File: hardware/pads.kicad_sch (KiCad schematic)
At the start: 21 parts, among them J10 M3, J13 M4, J20 LED, J21 5V, J22 BZ-, J23 CAM, J24 5V, J25 GND, J26 VHD, J27 GND, J28 TX0, J29 RX0, J31 USB, J32 CAM, J33 GND, J4 M1, J7 M2

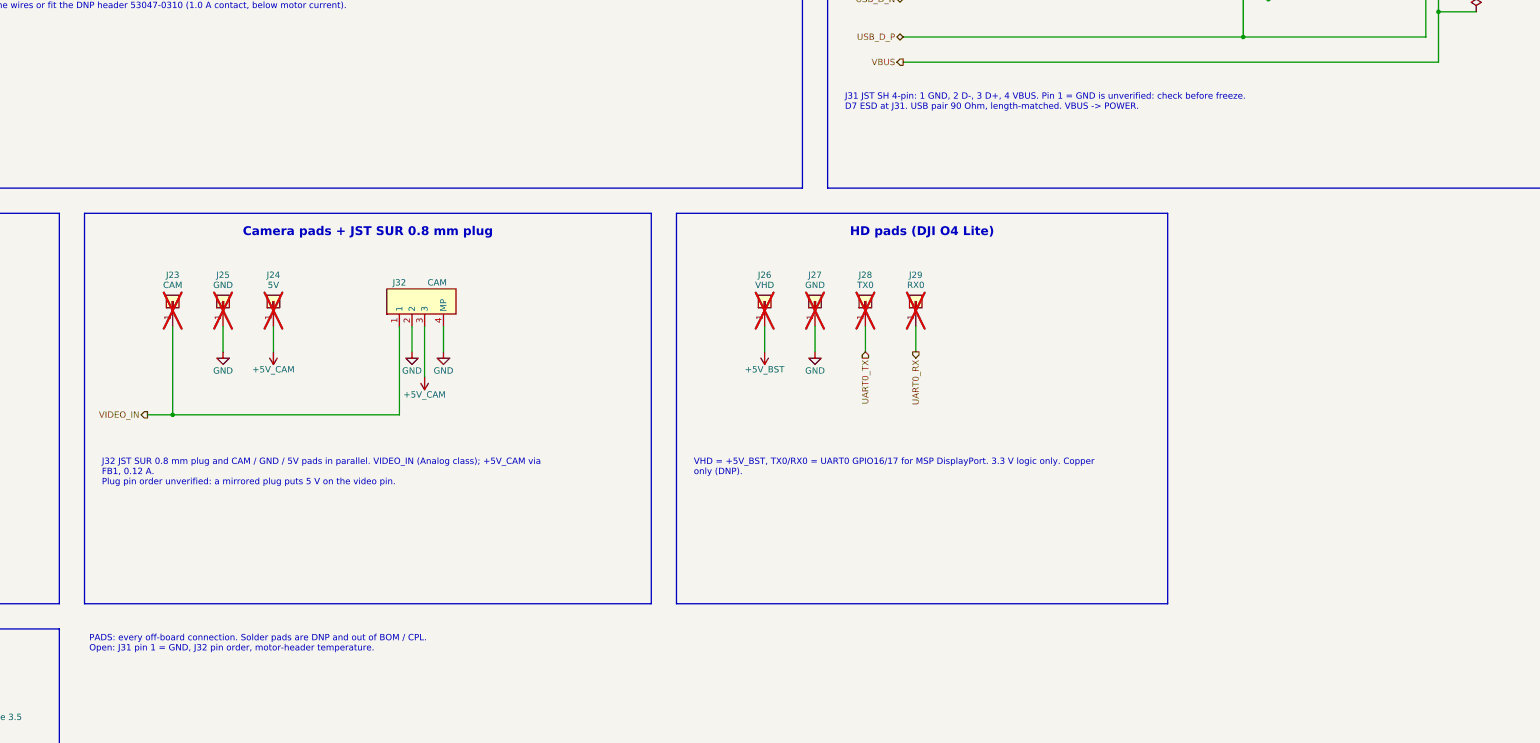
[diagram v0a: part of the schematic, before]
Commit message: Correct Whoop schematic and prepare component library for routing
Add local BMI270 bypassing, improve regulator capacitance margin, isolate
bidirectional DShot supply domains, and correct PA reference accuracy.
Remove Q28/R11 with matching firmware polarity and retain the proven
OpenFC-Lite OSD topology. Correct the receiver LED bypass rail.

Synchronize PCB connectivity, verify component pins and land patterns,
and provide firmware bindings plus placement/layer guidance. Replace stale
manual BOM and interface plans with schematic-derived exports.

Validation: ERC 0, seven netlist checks, 48 footprint checks, 22 rule
behavior cases, and PCB schematic parity 0. The parked PCB retains layout
DRC findings and 499 unconnected items; no manufacturing or flight release.
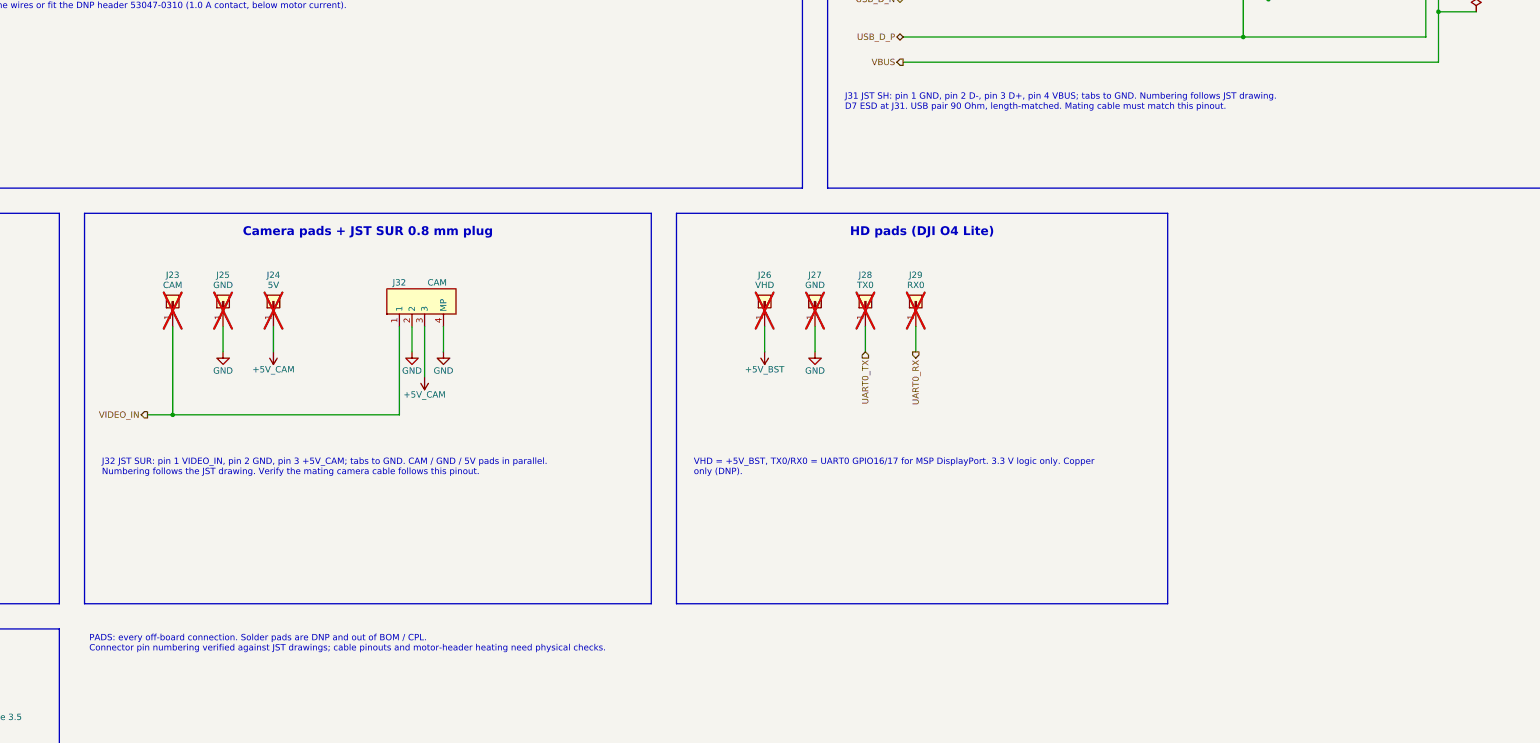
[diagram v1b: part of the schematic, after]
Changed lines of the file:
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@@
 		)
 	)
-	(text_box "J32 JST SUR 0.8 mm plug and CAM / GND / 5V pads in parallel. VIDEO_IN (Analog class); +5V_CAM via FB1, 0.12 A.\nPlug pin order unverified: a mirrored plug puts 5 V on the video pin."
+	(text_box "J32 JST SUR: pin 1 VIDEO_IN, pin 2 GND, pin 3 +5V_CAM; tabs to GND. CAM / GND / 5V pads in parallel.\nNumbering follows the JST drawing. Verify the mating camera cable follows this pinout."
 		(exclude_from_sim no)
 		(at 104.14 147.32 0)
@@
 		)
 	)
-	(text_box "J31 JST SH 4-pin: 1 GND, 2 D-, 3 D+, 4 VBUS. Pin 1 = GND is unverified: check before freeze.\nD7 ESD at J31. USB pair 90 Ohm, length-matched. VBUS -> POWER."
+	(text_box "J31 JST SH: pin 1 GND, pin 2 D-, pin 3 D+, pin 4 VBUS; tabs to GND. Numbering follows JST drawing.\nD7 ESD at J31. USB pair 90 Ohm, length-matched. Mating cable must match this pinout."
 		(exclude_from_sim no)
 		(at 254 73.66 0)
@@
 		)
 	)
-	(text_box "PADS: every off-board connection. Solder pads are DNP and out of BOM / CPL.\nOpen: J31 pin 1 = GND, J32 pin order, motor-header temperature."
+	(text_box "PADS: every off-board connection. Solder pads are DNP and out of BOM / CPL.\nConnector pin numbering verified against JST drawings; cable pinouts and motor-header heating need physical checks."
 		(exclude_from_sim no)
 		(at 101.6 182.88 0)

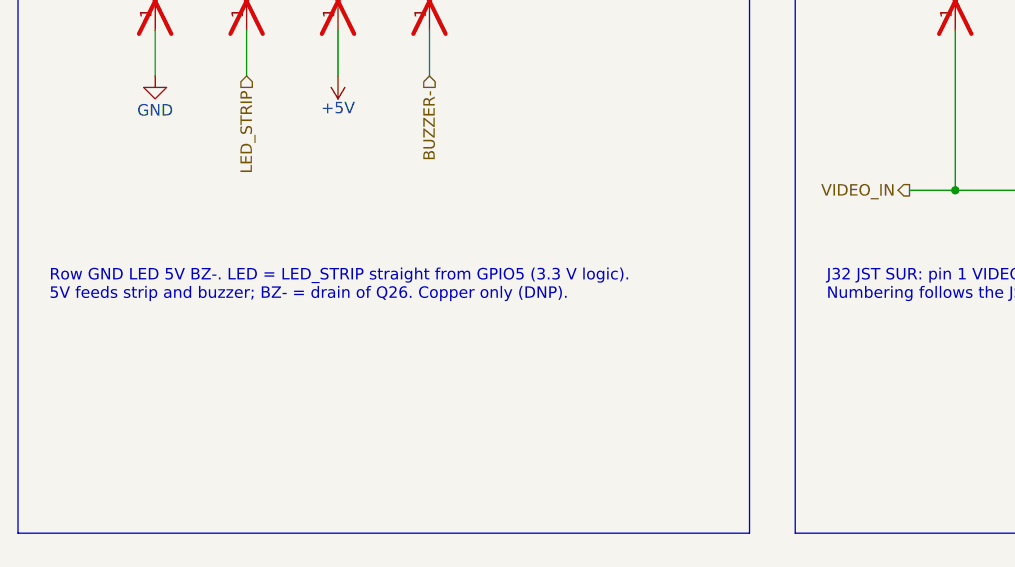
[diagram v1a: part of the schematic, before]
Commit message: Group RP2354A interfaces around the placed peripherals
Map motors 1-4 to GPIO7/6/5/4 for U24 north-side fanout, move gyro INT
to GPIO10, and put CRSF UART1 on GPIO24/25 beside the ESP32. Keep the
gyro SPI pad order, flash, OSD, ADC and dedicated system pins. Move the
status LEDs, strip and beeper to the released pins.

Synchronize the target, project library, PCB nets and schematic print; add
a schematic-to-firmware IO check with mux and PIO constraints. Remove eight
stale PCB footprints already absent from the owner schematic. Preserve all
retained placement and copper geometry.

Validation: 28 GPIOs match, 7 netlist checks and 22 rule behavior cases pass,
Betaflight builds, independent circuit/PCB review passes. ERC retains four
owner warnings; parity is zero. Board layout has 282 DRC findings and
499 unconnected items. This is not a hardware-tested release.
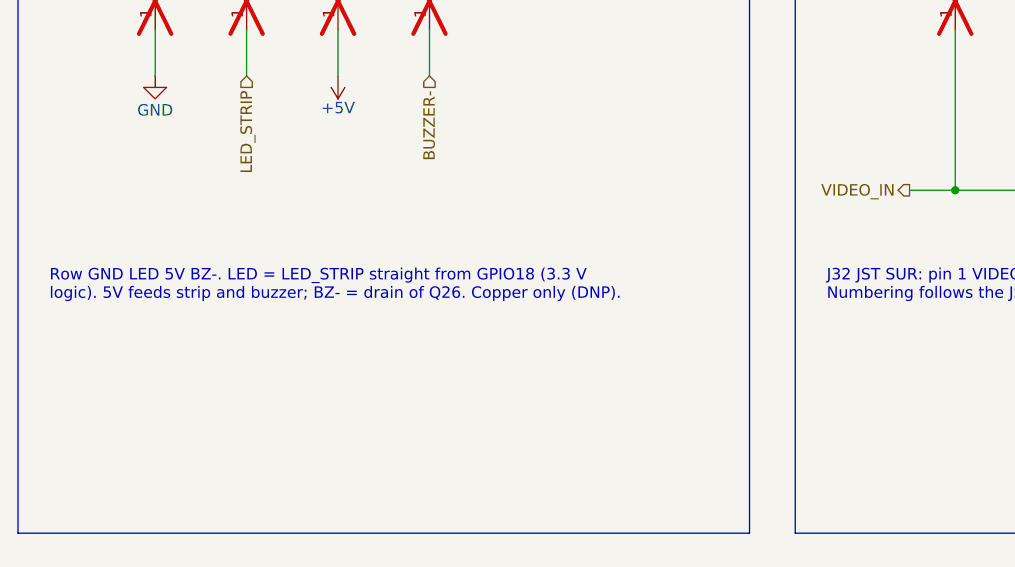
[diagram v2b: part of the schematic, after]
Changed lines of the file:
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@@
 		)
 	)
-	(text_box "Row GND LED 5V BZ-. LED = LED_STRIP straight from GPIO5 (3.3 V logic). 5V feeds strip and buzzer; BZ- = drain of Q26. Copper only (DNP)."
+	(text_box "Row GND LED 5V BZ-. LED = LED_STRIP straight from GPIO18 (3.3 V logic). 5V feeds strip and buzzer; BZ- = drain of Q26. Copper only (DNP)."
 		(exclude_from_sim no)
 		(at 17.78 147.32 0)
